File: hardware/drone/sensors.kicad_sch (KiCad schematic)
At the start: 17 parts, among them J2 BM08B-SRSS-TB_LF__SN_, U14 ICM-42688-P, U15 SAM_M10Q, U17 TXU0204, U19 BMP581, U22 LIS2MDL

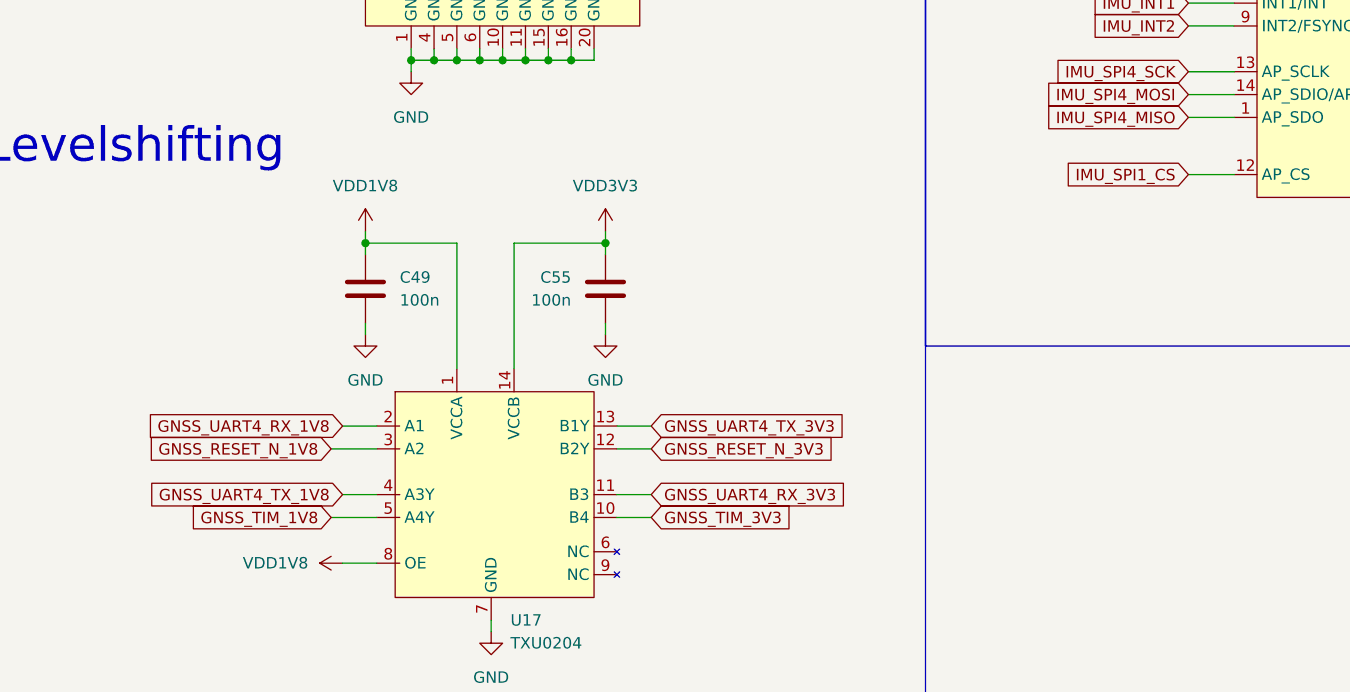
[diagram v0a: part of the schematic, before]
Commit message: Continued footprint assignments
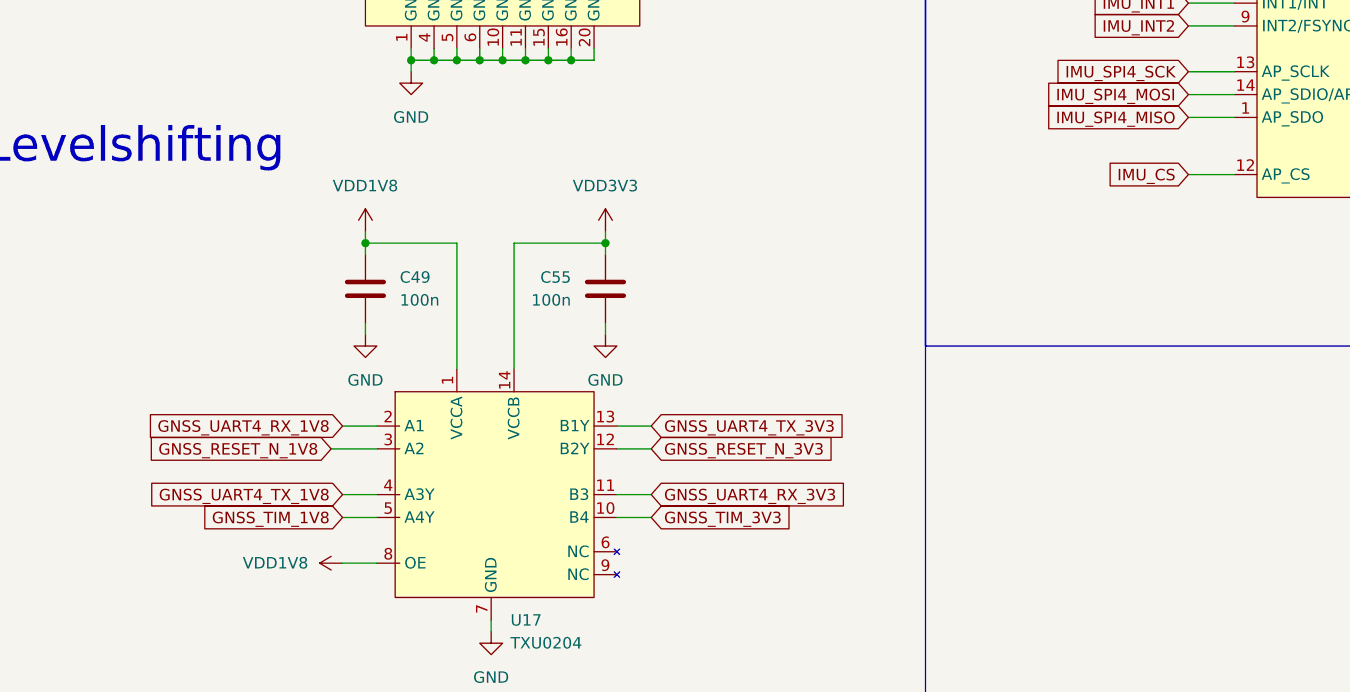
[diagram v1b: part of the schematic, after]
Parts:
- U14: footprint (none) -> ICM-42688-P:IIM42352
- U15: footprint (none) -> SAM-M10Q:SAMM10Q
- U17: footprint (none) -> TXU0204BQAR:TXU0204BQAR
- U19: footprint (none) -> BMP581:BMP581
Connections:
- net IMU_SPI1_CS renamed IMU_CS
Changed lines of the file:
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@@
 	(wire
 		(pts
-			(xy 66.04 146.05) (xy 71.12 146.05)
+			(xy 67.31 146.05) (xy 71.12 146.05)
 		)
 		(stroke
@@
 		)
 	)
-	(global_label "IMU_SPI1_CS"
+	(global_label "IMU_CS"
 		(shape input)
 		(at 161.29 107.95 180)
@@
 		)
 		(property "Intersheetrefs" "${INTERSHEET_REFS}"
-			(at 146.2096 107.95 0)
+			(at 151.471 107.95 0)
 			(hide yes)
 			(show_name no)
@@
 	(global_label "GNSS_TIM_1V8"
 		(shape input)
-		(at 66.04 146.05 180)
+		(at 67.31 146.05 180)
 		(fields_autoplaced yes)
 		(effects
@@
 		)
 		(property "Intersheetrefs" "${INTERSHEET_REFS}"
-			(at 49.5687 146.05 0)
+			(at 50.8387 146.05 0)
 			(hide yes)
 			(show_name no)
@@
 			)
 		)
-		(property "Footprint" ""
+		(property "Footprint" "SAM-M10Q:SAMM10Q"
 			(at 85.09 76.2 0)
 			(hide yes)
@@
 			)
 		)
-		(property "Footprint" ""
+		(property "Footprint" "TXU0204BQAR:TXU0204BQAR"
 			(at 83.82 143.51 0)
 			(hide yes)
@@
 			)
 		)
-		(property "Footprint" ""
+		(property "Footprint" "BMP581:BMP581"
 			(at 256.54 96.52 0)
 			(hide yes)
@@
 			)
 		)
-		(property "Footprint" ""
+		(property "Footprint" "ICM-42688-P:IIM42352"
 			(at 182.88 95.25 0)
 			(hide yes)

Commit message: More footprints
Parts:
- C119, C121, C82, C84, C90, C91: footprint (none) -> Capacitor_SMD:C_0201_0603Metric
- C120: footprint (none) -> Capacitor_SMD:CP_Elec_4x5.4
- C49, C55, C83: footprint (none) -> Capacitor_SMD:C_0402_1005Metric
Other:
- note added: "RVT1C100M0405 C3357"
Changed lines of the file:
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@@
 		)
 	)
+	(text "RVT1C100M0405\nC3357"
+		(exclude_from_sim no)
+		(at 298.958 73.406 90)
+		(effects
+			(font
+				(size 1.27 1.27)
+			)
+		)
+	)
 	(text "Barometer"
 		(exclude_from_sim no)
@@
 			)
 		)
-		(property "Footprint" ""
+		(property "Footprint" "Capacitor_SMD:C_0201_0603Metric"
 			(at 242.2652 82.55 0)
 			(hide yes)
@@
 			)
 		)
-		(property "Footprint" ""
+		(property "Footprint" "Capacitor_SMD:CP_Elec_4x5.4"
 			(at 305.7652 77.47 0)
 			(hide yes)
@@
 			)
 		)
-		(property "Footprint" ""
+		(property "Footprint" "Capacitor_SMD:C_0201_0603Metric"
 			(at 318.4652 77.47 0)
 			(hide yes)
@@
 			)
 		)
-		(property "Footprint" ""
+		(property "Footprint" "Capacitor_SMD:C_0201_0603Metric"
 			(at 230.8352 82.55 0)
 			(hide yes)
@@
 			)
 		)
-		(property "Footprint" ""
+		(property "Footprint" "Capacitor_SMD:C_0402_1005Metric"
 			(at 149.5552 72.39 0)
 			(hide yes)
@@
 			)
 		)
-		(property "Footprint" ""
+		(property "Footprint" "Capacitor_SMD:C_0201_0603Metric"
 			(at 160.9852 72.39 0)
 			(hide yes)
@@
 			)
 		)
-		(property "Footprint" ""
+		(property "Footprint" "Capacitor_SMD:C_0402_1005Metric"
 			(at 95.5548 124.46 0)
 			(hide yes)
@@
 			)
 		)
-		(property "Footprint" ""
+		(property "Footprint" "Capacitor_SMD:C_0201_0603Metric"
 			(at 329.8952 77.47 0)
 			(hide yes)
@@
 			)
 		)
-		(property "Footprint" ""
+		(property "Footprint" "Capacitor_SMD:C_0402_1005Metric"
 			(at 70.8152 124.46 0)
 			(hide yes)
@@
 			)
 		)
-		(property "Footprint" ""
+		(property "Footprint" "Capacitor_SMD:C_0201_0603Metric"
 			(at 172.4152 72.39 0)
 			(hide yes)

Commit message: More footprints
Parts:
- C118: footprint (none) -> Capacitor_SMD:C_0603_1608Metric
- C119, C121: footprint Capacitor_SMD:C_0201_0603Metric -> Capacitor_SMD:C_0603_1608Metric
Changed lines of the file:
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@@
 			)
 		)
-		(property "Footprint" "Capacitor_SMD:C_0201_0603Metric"
+		(property "Footprint" "Capacitor_SMD:C_0603_1608Metric"
 			(at 318.4652 77.47 0)
 			(hide yes)
@@
 			)
 		)
-		(property "Footprint" "Capacitor_SMD:C_0201_0603Metric"
+		(property "Footprint" "Capacitor_SMD:C_0603_1608Metric"
 			(at 329.8952 77.47 0)
 			(hide yes)
@@
 			)
 		)
-		(property "Footprint" ""
+		(property "Footprint" "Capacitor_SMD:C_0603_1608Metric"
 			(at 357.8352 105.41 0)
 			(hide yes)

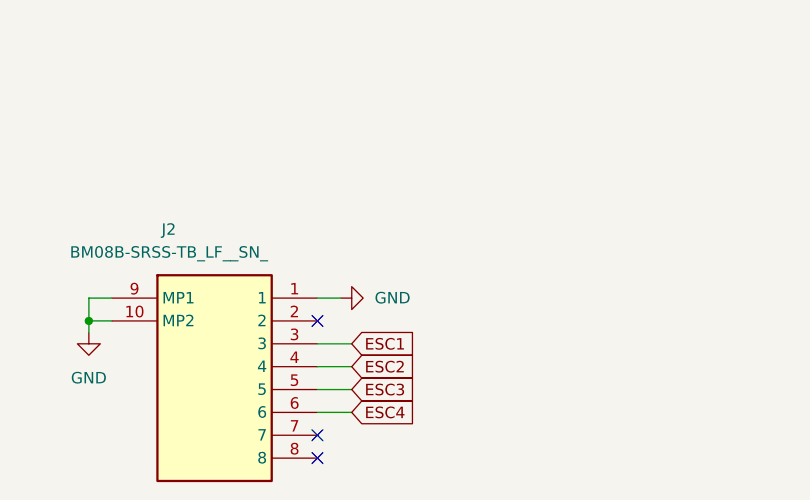
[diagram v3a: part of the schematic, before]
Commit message: Placed connectors and bucks
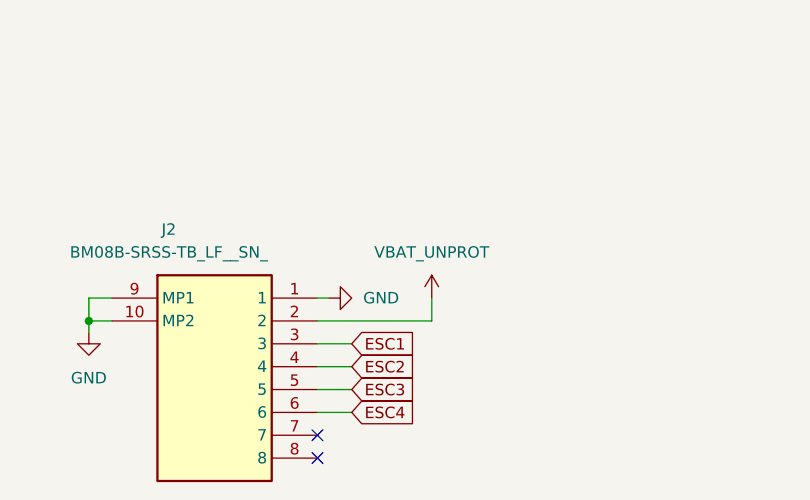
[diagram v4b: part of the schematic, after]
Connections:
- net VBAT_UNPROT: now reaches J2.2
- no-connect marks 8 -> 7
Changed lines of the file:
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@@
-	)
-	(no_connect
-		(at 85.09 208.28)
 	)
 	(no_connect
@@
 	(wire
 		(pts
+			(xy 85.09 208.28) (xy 97.79 208.28)
+		)
+		(stroke
+			(width 0)
+			(type default)
+		)
+	)
+	(wire
+		(pts
 			(xy 229.87 72.39) (xy 229.87 73.66)
 		)
@@
 	(wire
 		(pts
+			(xy 97.79 208.28) (xy 97.79 205.74)
+		)
+		(stroke
+			(width 0)
+			(type default)
+		)
+	)
+	(wire
+		(pts
 			(xy 254 73.66) (xy 254 81.28)
 		)
@@
 	(wire
 		(pts
-			(xy 85.09 205.74) (xy 87.63 205.74)
+			(xy 85.09 205.74) (xy 86.36 205.74)
 		)
 		(stroke
@@
 	(symbol
 		(lib_id "power:GND")
-		(at 87.63 205.74 90)
+		(at 86.36 205.74 90)
 		(unit 1)
 		(body_style 1)
@@
 		(fields_autoplaced yes)
 		(property "Reference" "#PWR0218"
-			(at 93.98 205.74 0)
+			(at 92.71 205.74 0)
 			(hide yes)
 			(show_name no)
@@
 		)
 		(property "Value" "GND"
-			(at 91.44 205.7399 90)
+			(at 90.17 205.7399 90)
 			(show_name no)
 			(do_not_autoplace no)
@@
 		)
 		(property "Footprint" ""
-			(at 87.63 205.74 0)
+			(at 86.36 205.74 0)
 			(hide yes)
 			(show_name no)
@@
 		)
 		(property "Datasheet" ""
-			(at 87.63 205.74 0)
+			(at 86.36 205.74 0)
 			(hide yes)
 			(show_name no)
@@
 		)
 		(property "Description" "Power symbol creates a global label with name \"GND\" , ground"
-			(at 87.63 205.74 0)
+			(at 86.36 205.74 0)
 			(hide yes)
 			(show_name no)
@@
 					(unit 1)
 				)
+			)
+		)
+	)
+	(symbol
+		(lib_id "power:VDD")
+		(at 97.79 205.74 0)
+		(unit 1)
+		(body_style 1)
+		(exclude_from_sim no)
+		(in_bom yes)
+		(on_board yes)
+		(in_pos_files yes)
+		(dnp no)
+		(fields_autoplaced yes)
+		(property "Reference" "#PWR0125"
+			(at 97.79 209.55 0)
+			(hide yes)
+			(show_name no)
+			(do_not_autoplace no)
+			(effects
+				(font
+					(size 1.27 1.27)
+				)
+			)
+		)
+		(property "Value" "VBAT_UNPROT"
+			(at 97.79 200.66 0)
+			(show_name no)
+			(do_not_autoplace no)
+			(effects
+				(font
+					(size 1.27 1.27)
+				)
+			)
+		)
+		(property "Footprint" ""
+			(at 97.79 205.74 0)
+			(hide yes)
+			(show_name no)
+			(do_not_autoplace no)
+			(effects
+				(font
+					(size 1.27 1.27)
+				)
+			)
+		)
+		(property "Datasheet" ""
+			(at 97.79 205.74 0)
+			(hide yes)
+			(show_name no)
+			(do_not_autoplace no)
+			(effects
+				(font
+					(size 1.27 1.27)
+				)
+			)
+		)
+		(property "Description" "Power symbol creates a global label with name \"VDD\""
+			(at 97.79 205.74 0)
+			(hide yes)
+			(show_name no)
+			(do_not_autoplace no)
+			(effects
+				(font
+					(size 1.27 1.27)
+				)
+			)
+		)
+		(pin "1"
+		)
+		(instances
+			(project "drone"
+				(path "/62c402a6-ed3f-446b-8423-821e9cc6908b/73325d99-70a4-4158-9179-bdcff983b262"
+					(reference "#PWR0125")
+					(unit 1)
+				)
